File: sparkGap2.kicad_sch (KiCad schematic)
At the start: 44 parts, among them J1 9V, J2 IN, J3 OUT, Q1 BS170, SW1 SPST, SW2 6-pin Footswitch, U1 TL072

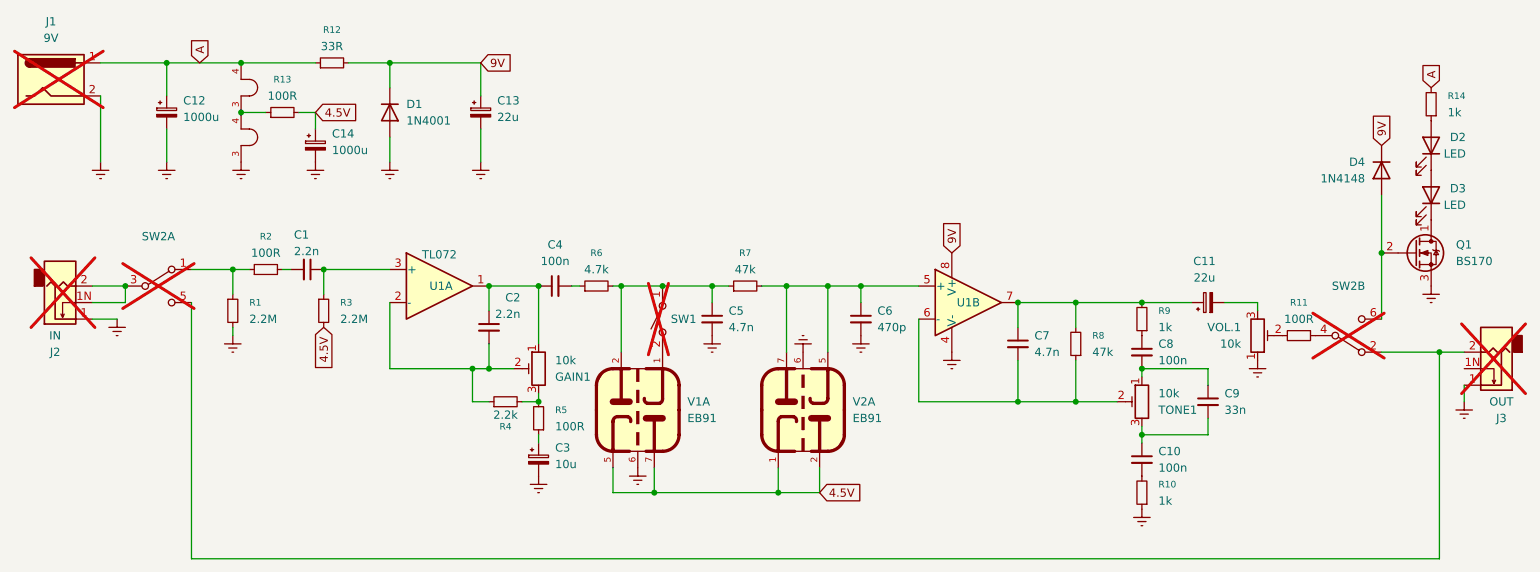
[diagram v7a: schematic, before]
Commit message: Clean up footprints and schematic to get rid of warnings
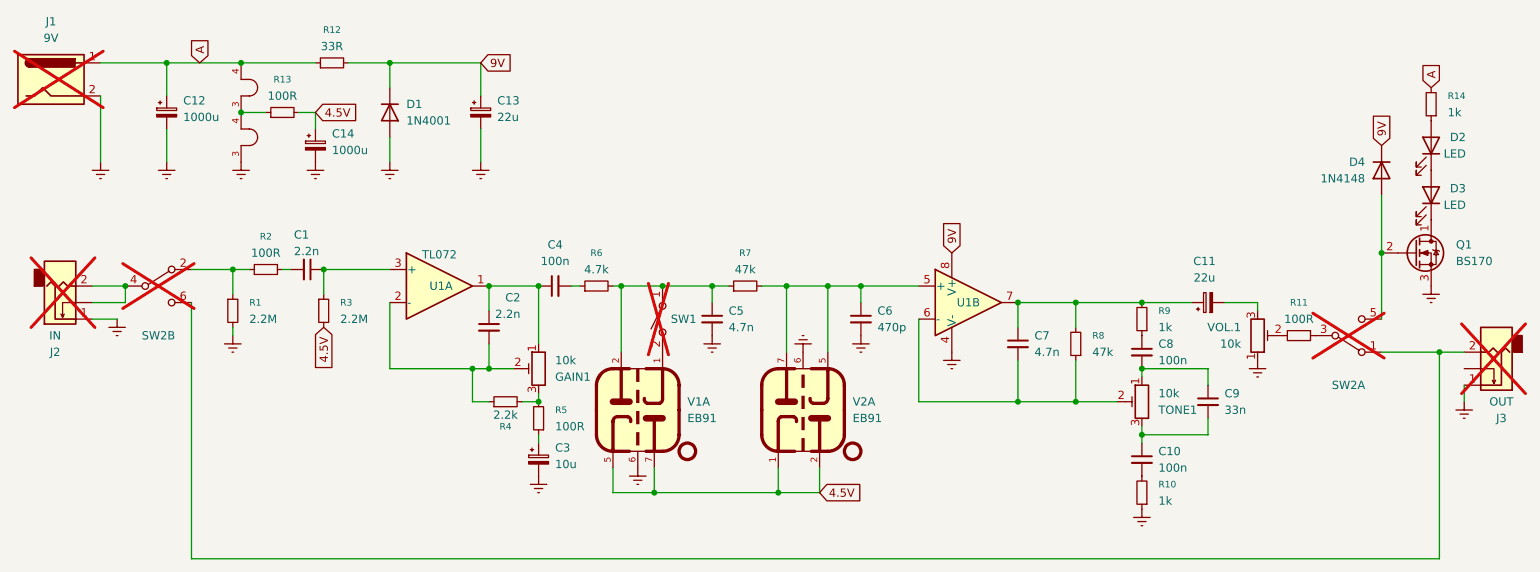
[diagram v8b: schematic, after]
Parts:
- added Mount1, Mount2: B9A Mount, SamacSys_Parts:B9A-shield-single-mount, symbol PCM_SparkFun-Hardware:Standoff
- J2, J3: symbol SamacSys_Parts:AudioJack2_Switch -> SamacSys_Parts:Jack2_off_board_Switch; now in the parts list
- SW2: footprint SamacSys_Parts:DPDT -> Connector_PinHeader_2.54mm:PinHeader_2x03_P2.54mm_Vertical
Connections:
- net at R1.1, R2.1: now also SW2.2; no longer SW2.1
- net at D4.2 (A), Q1.2 (G): now also SW2.5; no longer SW2.6
- net at SW2.4: now also J2.2; no longer R11.1
- new net: J3.2, SW2.1, SW2.6
- new net: R11.1, SW2.3
